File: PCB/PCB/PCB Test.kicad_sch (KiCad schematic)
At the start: 53 parts, among them J1 USB_C_Receptacle_USB2.0, J2 Conn_01x06, J3 BATT, Q1 DMN2056U, Q2 Si2329DS, Q3 DMN2056U, Q4 DMG9926UDM, SW1 SW_Push, SW2 SW_Push, U1 24FC64F, U2 STM32L052K6Tx, U3 TUSB320, U4 MIC5366-3.3YC5, U5 BQ297xy, U6 BQ24072RGT

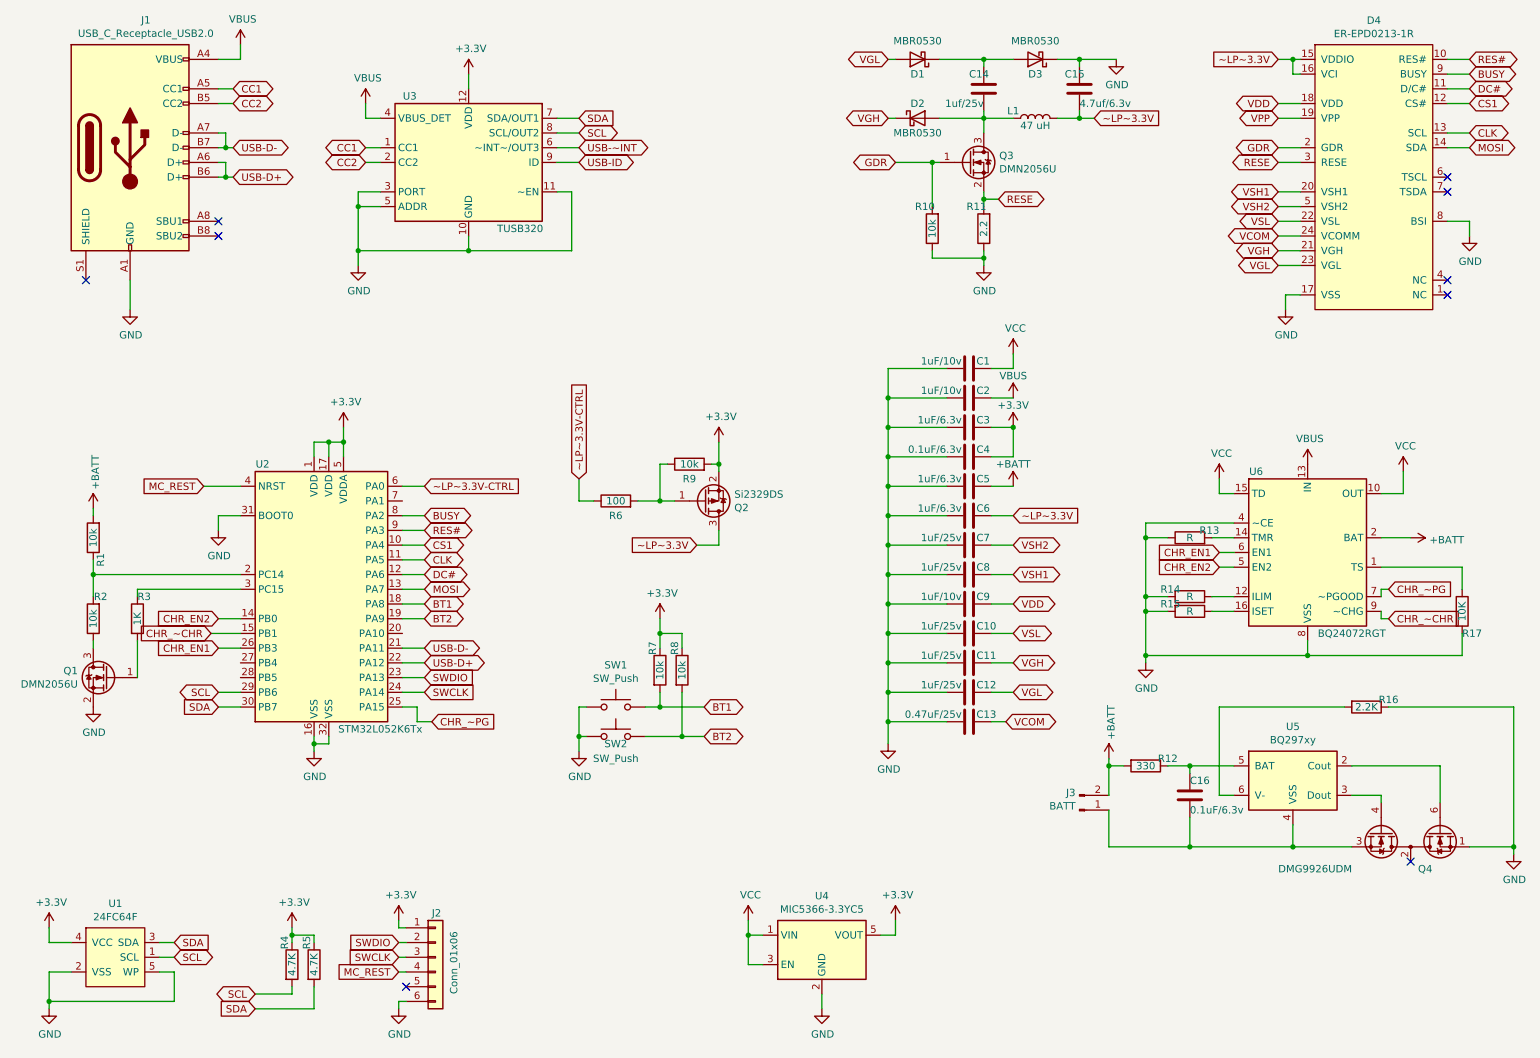
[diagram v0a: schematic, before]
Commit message: Updated schematic to Rev C
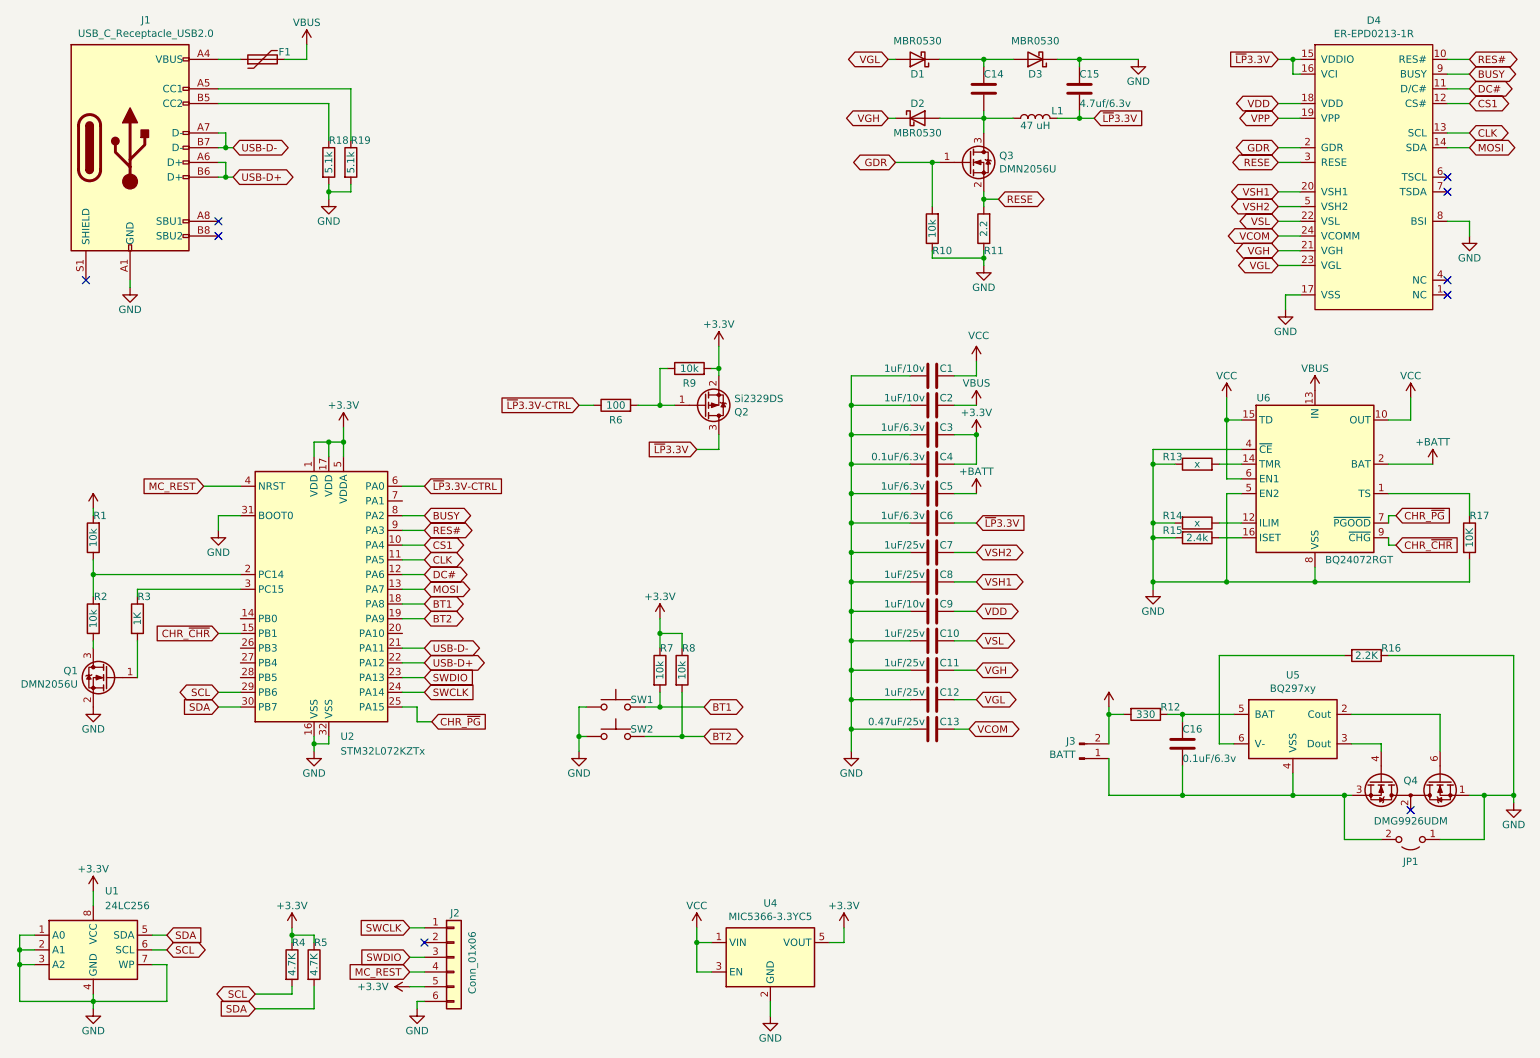
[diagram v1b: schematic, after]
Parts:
- removed U1: 24FC64F, Package_TO_SOT_SMD:SOT-23-5_HandSoldering, symbol PCB-Test-rescue:24FC64F-ProjectLibrary-PCB-Test-rescue-PCB-Test-rescue-PCB-Test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
- removed U2: STM32L052K6Tx, Package_QFP:LQFP-32_7x7mm_P0.8mm, symbol PCB-Test-rescue:STM32L052K6Tx-MCU_ST_STM32L0-PCB-Test-rescue
- removed U3: TUSB320, Package_DFN_QFN:Texas_X2QFN-12_1.6x1.6mm_P0.4mm, symbol PCB-Test-rescue:TUSB320-Interface_USB-PCB-Test-rescue
- added F1: Polyfuse, Fuse:Fuse_1210_3225Metric_Pad1.42x2.65mm_HandSolder, symbol Device:Polyfuse
- added JP1: (no value), symbol Jumper:Jumper_2_Open
- added R18, R19: 5.1k, Resistor_SMD:R_0805_2012Metric_Pad1.20x1.40mm_HandSolder, symbol Device:R
- added U1: 24LC256, Package_SO:MSOP-8_3x3mm_P0.65mm, symbol Memory_EEPROM:24LC256
- added U2: STM32L072KZTx, Package_QFP:LQFP-32_7x7mm_P0.8mm, symbol MCU_ST_STM32L0:STM32L072KZTx
- C10, C11, C12, C13, C15, C16, C2, C3, C4, C5, C6, C7, C8, C9: footprint Capacitor_SMD:C_0805_2012Metric_Pad1.15x1.40mm_HandSolder -> Capacitor_SMD:C_0805_2012Metric_Pad1.18x1.45mm_HandSolder
- C14: value 1uf/25v -> (none); footprint Capacitor_SMD:C_0805_2012Metric_Pad1.15x1.40mm_HandSolder -> Capacitor_SMD:C_0805_2012Metric_Pad1.18x1.45mm_HandSolder
- R1, R10, R11, R12, R16, R17, R2, R3, R4, R5, R6, R7, R8, R9: footprint Resistor_SMD:R_0805_2012Metric_Pad1.15x1.40mm_HandSolder -> Resistor_SMD:R_0805_2012Metric_Pad1.20x1.40mm_HandSolder
- R13, R14: value R -> x; footprint Resistor_SMD:R_0805_2012Metric_Pad1.15x1.40mm_HandSolder -> Resistor_SMD:R_0805_2012Metric_Pad1.20x1.40mm_HandSolder
- R15: value R -> 2.4k; footprint Resistor_SMD:R_0805_2012Metric_Pad1.15x1.40mm_HandSolder -> Resistor_SMD:R_0805_2012Metric_Pad1.20x1.40mm_HandSolder
- SW1, SW2: value SW_Push -> (none); footprint Button_Switch_THT:SW_Tactile_SPST_Angled_PTS645Vx83-2LFS -> (none)
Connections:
- net CHR_EN1 is gone; now on net VCC: U6.6 (EN1)
- net CHR_EN2 is gone; now on net GND: U6.5 (EN2)
- net +3V3: now also J2.5 (Pin_5), U1.8 (VCC), U2.1 (VDD), U2.17 (VDD), U2.5 (VDDA); no longer J2.1 (Pin_1)
- net BT1: now also U2.18 (PA8)
- net BT2: now also U2.19 (PA9)
- net BUSY: now also U2.8 (PA2)
- net CLK: now also U2.11 (PA5)
- net CS1: now also U2.10 (PA4)
- net DC#: now also U2.12 (PA6)
- net GND: now also JP1.1 (A), R18.2, R19.2, U1.1 (A0), U1.2 (A1), U1.3 (A2), U1.4 (GND), U1.7 (WP), U2.16 (VSS), U2.31 (BOOT0), U2.32 (VSS)
- net MC_REST: now also U2.4 (NRST)
- net MOSI: now also U2.13 (PA7)
- net RES#: now also U2.9 (PA3)
- net SCL: now also U1.6 (SCL), U2.29 (PB6)
- net SDA: now also U1.5 (SDA), U2.30 (PB7)
- net SWCLK: now also J2.1 (Pin_1), U2.24 (PA14); no longer J2.3 (Pin_3)
- net SWDIO: now also J2.3 (Pin_3), U2.23 (PA13); no longer J2.2 (Pin_2)
- net USB-D+: now also U2.22 (PA12)
- net USB-D-: now also U2.21 (PA11)
- net VBUS: now also F1.2; no longer J1.A4 (VBUS), J1.A9 (VBUS), J1.B4 (VBUS), J1.B9 (VBUS)
- net at C16.2, J3.1 (Pin_1), Q4.3 (S2)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: now also JP1.2 (B)
- net at R1.1, R2.2: now also U2.2 (PC14)
- net at R3.1: now also U2.3 (PC15)
- net CC1: no longer names the net of J1.A5 (CC1)
- net CC1: now also R19.1
- net CC2: no longer names the net of J1.B5 (CC2)
- net CC2: now also R18.1
- net CHR_~CHR renamed CHR_~{CHR}
- net CHR_~{CHR}: now also U2.15 (PB1)
- net CHR_~PG renamed CHR_~{PG}
- net CHR_~{PG}: now also U2.25 (PA15)
- net ~LP~3.3V renamed ~{LP}3.3V
- net ~LP~3.3V-CTRL renamed ~{LP}3.3V-CTRL
- net ~{LP}3.3V-CTRL: now also U2.6 (PA0)
- new net: F1.1, J1.A4 (VBUS), J1.A9 (VBUS), J1.B4 (VBUS), J1.B9 (VBUS)
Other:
- moved on the sheet: C1, C10, C11, C12, C13, C16, C2, C3, C4, C5, C6, C7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
